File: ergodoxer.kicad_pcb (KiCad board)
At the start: 2 copper layers, 203.2 x 181.7 mm, 106 parts, among them J1 USB_C_Receptacle, SW1 SW_Push, SW10 SW_Push, SW11 SW_Push, SW12 SW_Push, SW13 SW_Push, SW14 SW_Push, SW15 SW_Push, SW16 SW_Push, SW17 SW_Push, SW18 SW_Push, SW19 SW_Push, SW2 SW_Push, SW20 SW_Push, SW21 SW_Push, SW22 SW_Push, SW23 SW_Push, SW24 SW_Push, SW25 SW_Push, SW26 SW_Push, SW27 SW_Push, SW28 SW_Push, SW29 SW_Push, SW3 SW_Push, SW30 SW_Push, SW31 SW_Push, SW32 SW_Push, SW33 SW_Push, SW34 SW_Push, SW35 SW_Push, SW36 SW_Push, SW37 SW_Push, SW38 SW_Push, SW39 SW_Push, SW4 SW_Push, SW40 SW_Push, SW41 SW_Push, SW43 SW_Push, SW44 SW_Push, SW45 SW_Push, SW46 SW_Push, SW47 SW_Push, SW48 SW_Push, SW49 SW_Push, SW5 SW_Push, SW50 SW_Push, SW51 SW_Push, SW52 SW_Push, SW53 SW_Push, SW6 SW_Push, SW7 SW_Push, SW8 SW_Push, SW9 SW_Push, U1 proton_c

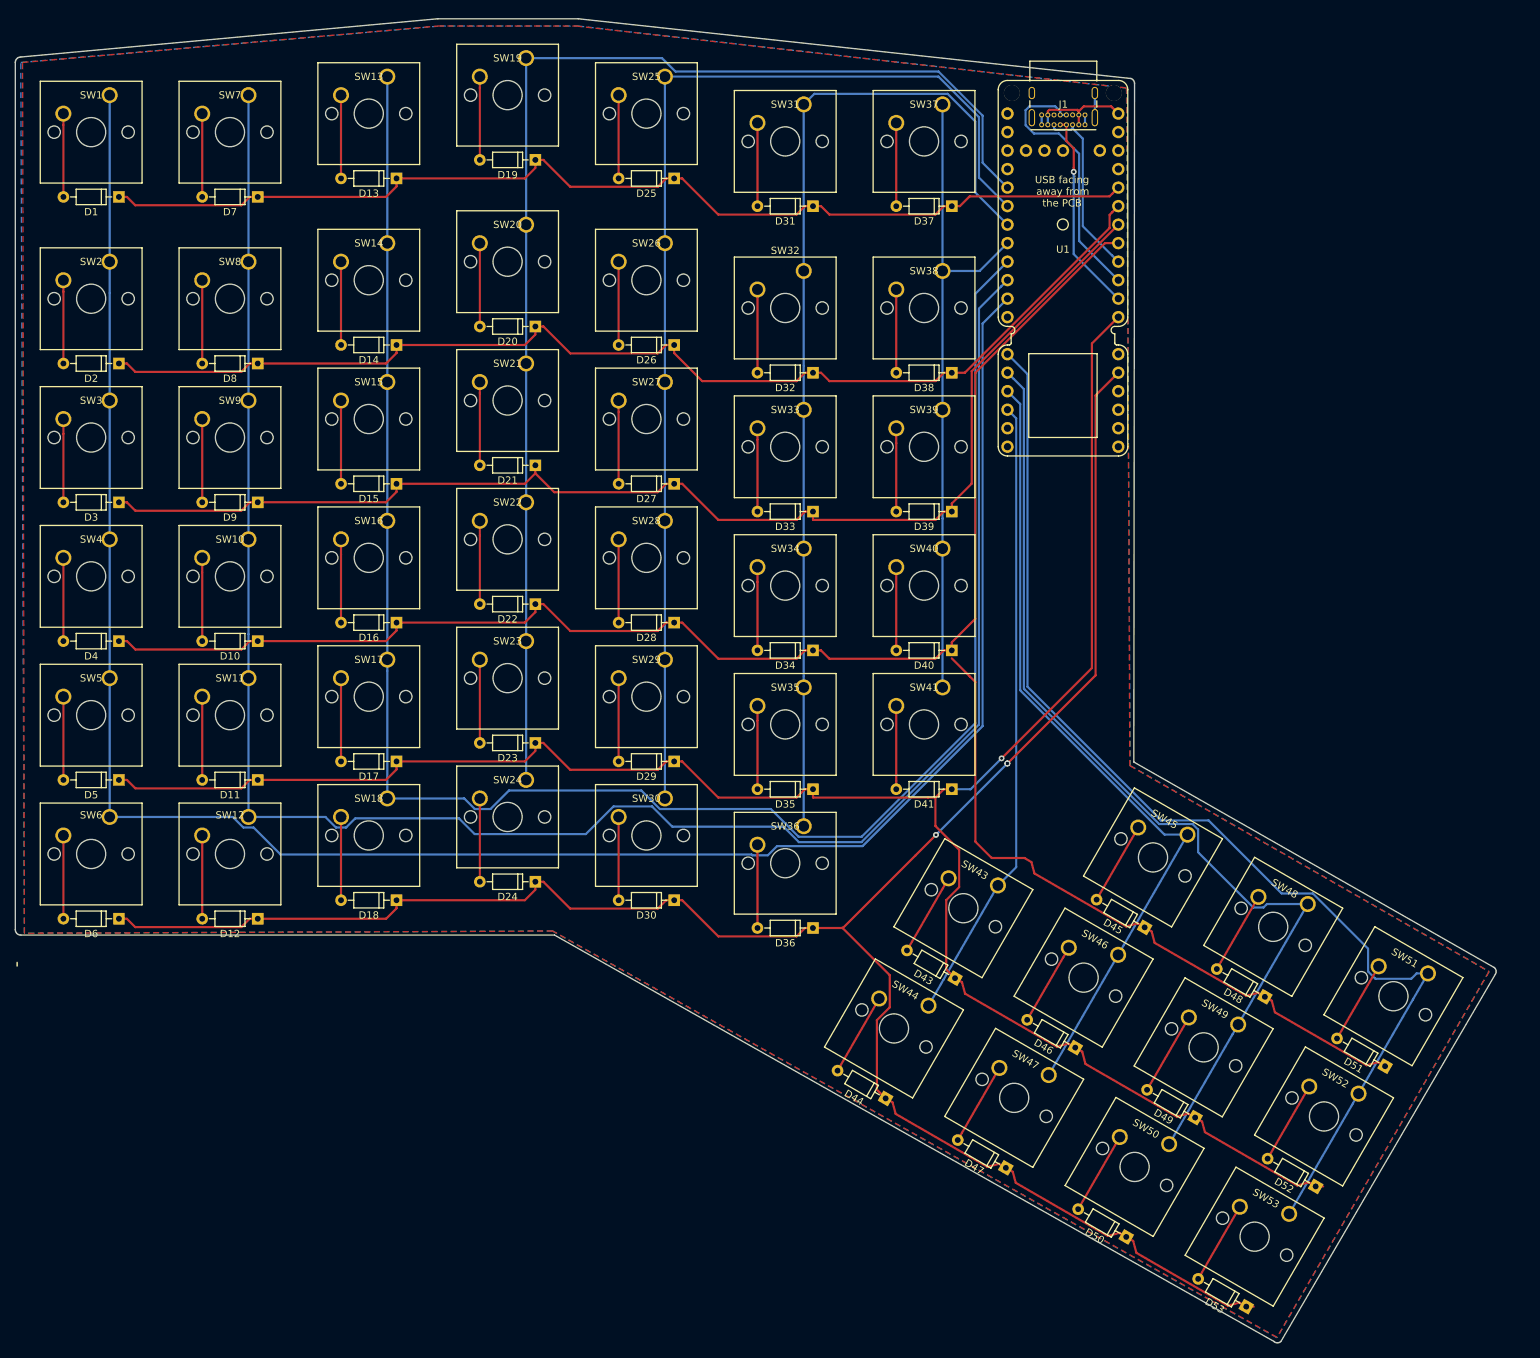
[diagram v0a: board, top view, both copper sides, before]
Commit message: Flip switches upside down
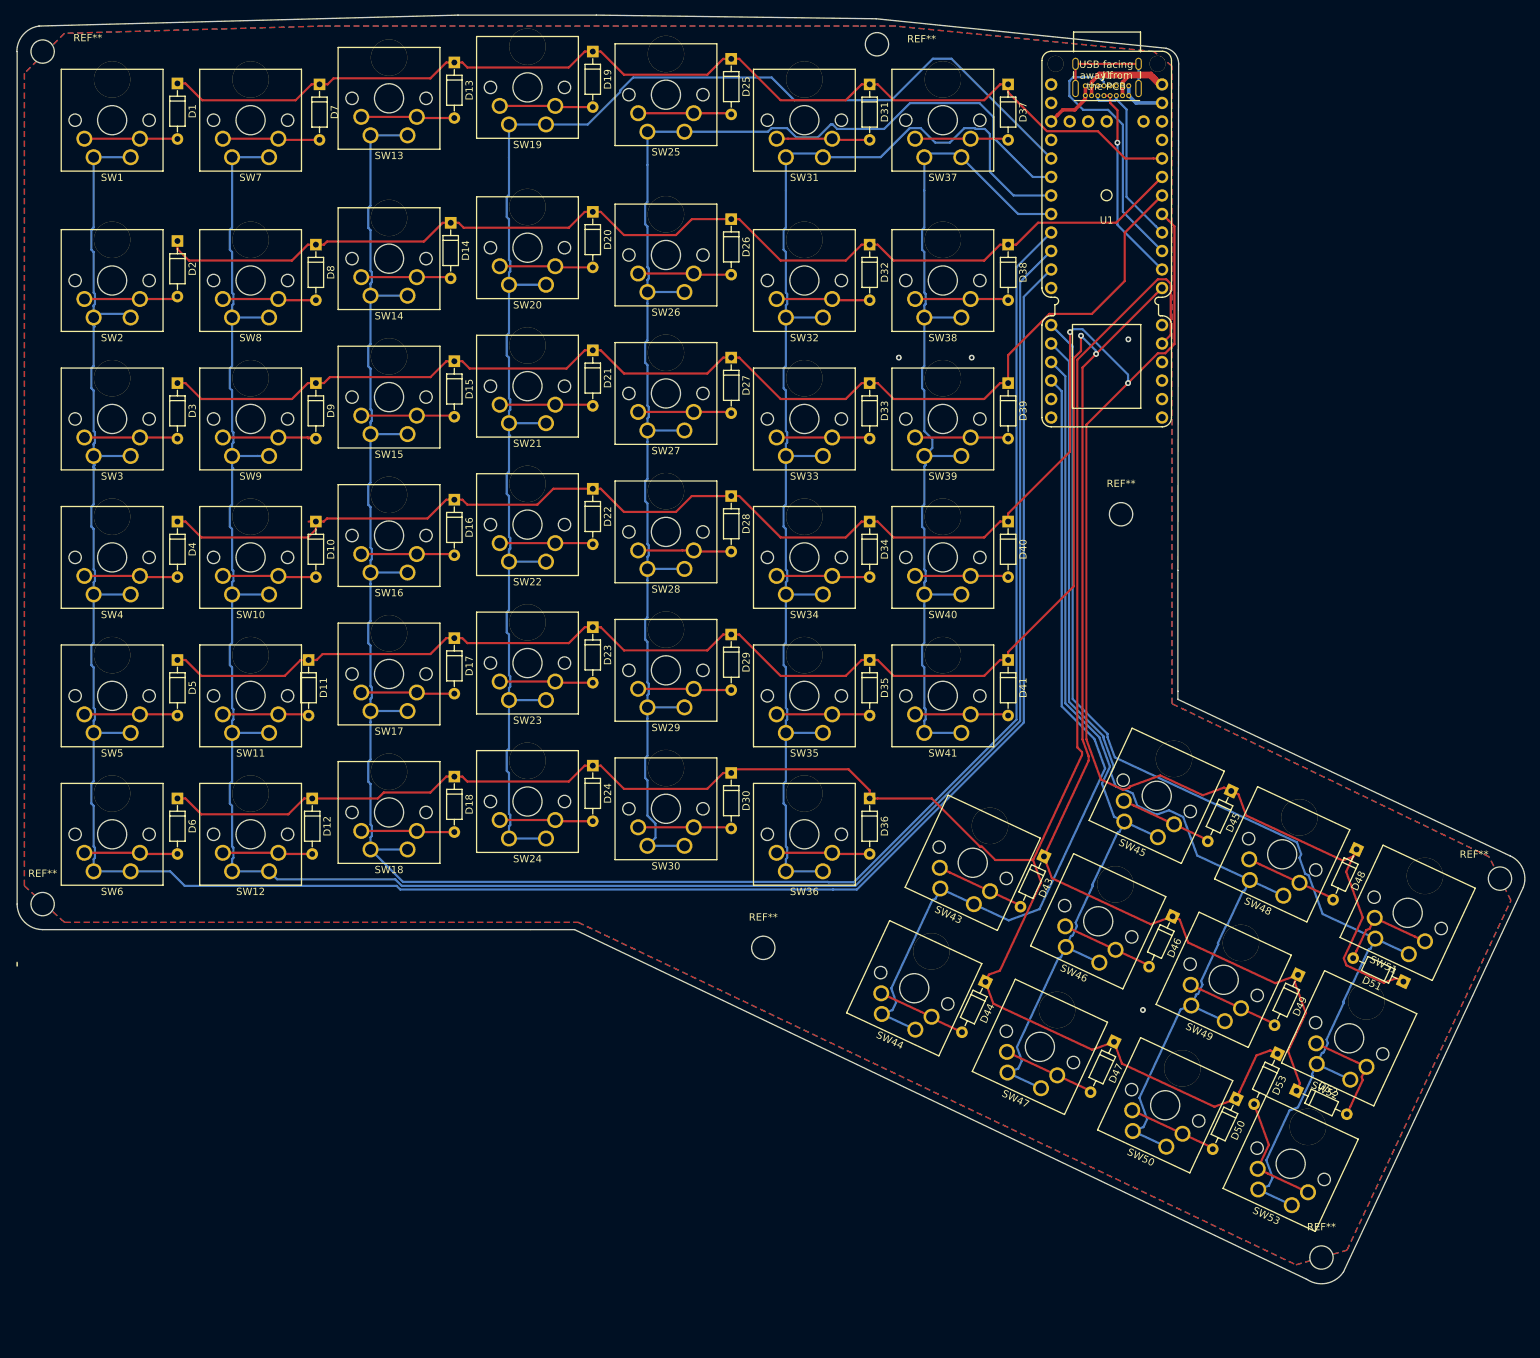
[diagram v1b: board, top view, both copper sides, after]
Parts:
- added REF**: MountingHole_3.2mm_M3, Mounting_Holes:MountingHole_3.2mm_M3, F.Cu at (215.0, 88.0)
- added REF**: MountingHole_3.2mm_M3, Mounting_Holes:MountingHole_3.2mm_M3, F.Cu at (181.5, 23.5)
- added REF**: MountingHole_3.2mm_M3, Mounting_Holes:MountingHole_3.2mm_M3, F.Cu at (67.0, 24.5)
- added REF**: MountingHole_3.2mm_M3, Mounting_Holes:MountingHole_3.2mm_M3, F.Cu at (67.0, 141.5)
- added REF**: MountingHole_3.2mm_M3, Mounting_Holes:MountingHole_3.2mm_M3, F.Cu at (165.9, 147.5)
- added REF**: MountingHole_3.2mm_M3, Mounting_Holes:MountingHole_3.2mm_M3, F.Cu at (242.5, 190.0)
- added REF**: MountingHole_3.2mm_M3, Mounting_Holes:MountingHole_3.2mm_M3, F.Cu at (267.0, 138.0)
- SW1, SW10, SW11, SW12, SW13, SW14, SW15, SW16, SW17, SW18, SW19, SW2, SW20, SW21, SW22, SW23, SW24, SW25, SW26, SW27, SW28, SW29, SW3, SW30, SW31, SW32, SW33, SW34, SW35, SW36, SW37, SW38, SW39, SW4, SW40, SW41, SW43, SW44, SW45, SW46, SW47, SW48, SW49, SW5, SW50, SW51, SW52, SW53, SW6, SW7, SW8, SW9: footprint Button_Switch_keyboard:SW_Cherry_MX_1.00u_PCB -> switches:SW_Cherry_MX_1.00u_PCB_dual
- U1: value proton_c -> Proton_C
- moved D53 35.0 mm to (236.5, 162.0), turned to 245 degrees
- moved D50 24.2 mm to (230.8, 168.2), turned to 245 degrees
- moved D49 24.1 mm to (239.3, 151.2), turned to 245 degrees
- moved D48 23.8 mm to (247.3, 134.0), turned to 245 degrees
- moved D47 22.8 mm to (214.0, 160.4), turned to 245 degrees
- moved D46 22.4 mm to (222.1, 143.2), turned to 245 degrees
- moved D45 22.2 mm to (230.1, 126.0), turned to 245 degrees
- moved D44 21.1 mm to (196.4, 152.2), turned to 245 degrees
- moved D43 20.7 mm to (204.4, 135.0), turned to 245 degrees
- moved D36 19.4 mm to (180.5, 127.0), turned to 270 degrees
- moved D35 19.4 mm to (180.5, 108.0), turned to 270 degrees
- moved D41 19.3 mm to (199.5, 108.0), turned to 270 degrees
- moved D34 19.3 mm to (180.5, 89.0), turned to 270 degrees
- moved D40 19.3 mm to (199.5, 89.0), turned to 270 degrees
- moved D33 19.3 mm to (180.5, 70.0), turned to 270 degrees
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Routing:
- net column3: track 255.7 -> 299.4 mm
- net column1: track 288.5 -> 329.8 mm
- net column4: track 176.3 -> 214.0 mm
- net row4: track 284.7 -> 319.6 mm, vias 0 -> 2
- net column2: track 275.0 -> 309.7 mm
- net column5: track 158.3 -> 190.6 mm
- net column7: track 90.5 -> 122.7 mm
- net row5: track 289.0 -> 321.0 mm, vias 1 -> 2
- net column8: track 85.9 -> 117.3 mm
- net column6: track 140.8 -> 172.0 mm
- net Net-(J1-PadS1): track 3.38 -> 15.4 mm
- net GND: track 2.70 -> 14.1 mm, vias 0 -> 4
- net VBUS: track 14.2 -> 25.6 mm
- net column9: track 111.0 -> 122.3 mm
- net row3: track 173.2 -> 163.7 mm
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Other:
- board size 203.2 x 181.7 mm -> 207 x 174.1 mm
- net class power added: clearance 0.2, trace_width 0.5, via_dia 0.8, via_drill 0.4
